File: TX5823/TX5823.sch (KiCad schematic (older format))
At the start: 8 parts

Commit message: an Schaltplan weitergearbeitet
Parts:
- added C? (x10): 100nF, Capacitors_SMD:C_0402, symbol C
- added C? (x5): 1uF, Capacitors_SMD:C_0603, symbol C
- added C?: 10uF, Capacitors_SMD:C_1206, symbol C
- added C?: Cboot, symbol C
- added C? (x2): 47uF, symbol CP2
- added C?: Cout, symbol CP2
- added C?: Cvccx, symbol C
- added C?: 100nF, symbol C
- added C?: Cvcc, symbol C
- added C?: Ccomp2, symbol C
- added C?: Ccomp, symbol C
- added C?: Css, symbol C
- added C?: Cramp, symbol C
- added C?: Cinx, symbol C
- added C?: Cin, symbol C
- added D?: LED, symbol LED
- added D? (x4): DIODESCH, symbol DIODESCH
- added L?: 15uH, symbol INDUCTOR
- added P?: CONN_02X03, symbol CONN_02X03
- added Q?: MOSFET_N, symbol MOSFET_N
- added Q? (x2): MOS_N, symbol MOS_N
- added R?: 10, symbol R
- added R?: 100, Resistors_SMD:R_1206, symbol R
- added R? (x4): open, Resistors_SMD:R_0402, symbol R
- added R?: 10k, symbol R
- added R?: 330, symbol R
- added R? (x2): 75, symbol R
- added R?: Rsense, symbol R
- added R?: Rfbt, symbol R
- added R?: Rfbb, symbol R
- added R?: Rcomp, symbol R
- added R?: Rt, symbol R
- added R?: Renable, symbol R
- added R?: Ruv1, symbol R
- added R?: Ruv2, symbol R
- added RP?: R_PACK4, symbol R_PACK4
- added SW?: SW_PUSH, symbol SW_PUSH
- added X?: 27MHz, symbol CRYSTAL_SMD
- added Y?: 16MHz, symbol RESONATEUR
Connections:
- net +3.3V: now also IC?.8 (VCC), U?.1 (SNS), U?.15 (OUT), U?.16 (OUT), U?.4 (3,3V_VCC), C?.1, C?.1, C?.1, C?.1, C?.1
- net GND: now reaches U?.3 (GND)
- net GND: now also IC?.21 (GND), IC?.3 (GND), IC?.4 (GND), IC?.5 (GND), U?.10 (1,6V), U?.13 (CSG), U?.14 (PGND), U?.17 (EP), U?.20 (AGND), U?.21 (EP), U?.23 (PGND), U?.27, U?.4 (DGND), U?.5 (GND), U?.6 (AGND), U?.7 (GND), U?.8 (400mV), U?.9 (800mV), U?.9 (GND), C?.1, C?.2, C?.2, C?.2, C?.2, C?.2, C?.2, C?.2, C?.2, C?.2, C?.2, C?.2, C?.2, C?.2, C?.2, C?.2, C?.2, C?.2, C?.2, C?.2, D?.2 (K), P?.6 (P6), Q?.S, Q?.S, R?.1, R?.2, R?.2, R?.2, R?.2, R?.2, R?.2, R?.2, SW?.2, Y?.2
- net SCK: now reaches U?.10 (SCLK)
- net SCK: now also IC?.17 ((PCINT5/SCK)PB5), P?.3 (P3), R?.1
- net MISO: now reaches U?.11 (SDOUT)
- net MISO: now also IC?.16 ((PCINT4/MISO)PB4), P?.1 (P1)
- net LOS: now reaches U?.12 (LOS)
- net LOS: now also RP?.7 (R2)
- net VSYNC: now reaches U?.17 (~VSYNC)
- net VSYNC: now also IC?.32 ((PCINT18/INT0)PD2), RP?.6 (R3)
- net HSYNC: now reaches U?.18 (~HSYNC)
- net HSYNC: now also RP?.5 (R4)
- net RESET: now reaches U?.19 (~RESET)
- net RESET: now also IC?.29 ((PCINT14/~RESET~)PC6), C?.1, P?.5 (P5), R?.2, SW?.1
- net +5V: now reaches U?.21 (AVDD)
- net +5V: now also IC?.18 (AVCC), IC?.4 (VCC), IC?.6 (VCC), U?.12 (EN), U?.13 (IN), U?.14 (IN), U?.24 (PVDD), U?.3 (DVDD), C?.1, C?.1, C?.1, C?.1, C?.1, C?.1, C?.1, P?.2 (P2), R?.1, R?.1, R?.1, RP?.2 (P2), RP?.3 (P3), RP?.4 (P4)
- net at U?.22 (VIN): now also C?.2
- net at U?.25 (SAG): now also C?.2
- net at U?.26 (VOUT): now also C?.2
- net at U?.5 (CLKIN): now also X?.1
- net at U?.6 (XFB): now also X?.2
- net CLKOUT: now reaches U?.7 (CLKOUT)
- net SSOD-IN: now reaches U?.8 (~CS)
- net MOSI: now reaches U?.9 (SDIN)
- net MOSI: now also IC?.15 ((PCINT3/OC2A/MOSI)PB3), P?.4 (P4)
- net PAL: now reaches IC?.1 ((PCINT19/OC2B/INT1)PD3)
- net PAL: now also R?.2
- net SSOSD-IN: now reaches IC?.10 ((PCINT22/OC0A/AIN0)PD6)
- net at IC?.20 (AREF): now also C?.1
- net RXI: now reaches IC?.30 ((PCINT16/RXD)PD0)
- net TXO: now reaches IC?.31 ((PCINT17/TXD)PD1)
- net at IC?.7 ((PCINT6/XTAL1/TOSC1)PB6): now also Y?.3
- net at IC?.8 ((PCINT7/XTAL2/TOSC2)PB7): now also Y?.1
- net at IC?.2 (PB3(CLKI/ADC3/PCINT3)): now also R?.1
- net PWM_in: now reaches IC?.6 (PB1(MISO/AIN1/OC0B/INT0/PCINT1))
- net at U?.11 (SS): now also C?.1
- net at U?.2 (FB): now also C?.2, C?.2
- net at U?.4 (50mV): now also R?.1
- net at U?.5 (100mV): now also R?.1
- net at U?.6 (200mV): now also R?.1
- net at U?.1 (VIN): now also C?.1, C?.1, Q?.D, R?.1, R?.1
- net at U?.10 (VOUT): now also C?.1, D?.2 (K), D?.2 (K), R?.1
- net at U?.12 (CS): now also D?.1 (A), D?.1 (A), R?.1
- net at U?.15 (LO): now also Q?.G
- net at U?.16 (VCC): now also C?.1
- net at U?.17 (VCCX): now also C?.2
- net at U?.18 (HB): now also C?.2
- net at U?.19 (HO): now also Q?.G
- net at U?.2 (UVLO): now also R?.1, R?.2
- net at U?.20 (HS): now also C?.1, D?.2 (K), D?.2 (K), L?.1, Q?.S
- net at U?.3 (RT): now also R?.1
- net at U?.4 (EN): now also R?.2
- net at U?.5 (RAMP): now also C?.1
- net at U?.7 (SS): now also C?.1
- net at U?.8 (FB): now also C?.2, C?.2, R?.2, R?.2
- net at U?.9 (COMP): now also C?.1, R?.1
- new net: Q?.G, R?.2
- new net: D?.1 (A), R?.2
- new net: D?.1 (A), D?.1 (A), L?.2, Q?.D
- new net: C?.1, C?.1, R?.2
- new net: C?.1, R?.2
- new net DTR: C?.2
- new net IR_LED+: R?.2
- new net IR_LED-: Q?.D
- new net VIN: C?.1, R?.1
- new net VOUT: R?.1
- no-connect marks 0 -> 17
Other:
- note added: "12V Buck Boost\nVinMin 8V\nVinMax=30V\nVout=12V\nIout= 2A"
- note added: "5V Stepdown"
- note added: "FPV Sender\nund 3,3V"
- note added: "OSD"
- note removed: "5V_Stepdown"
- note removed: "TODO\nBOOST\nEP anpassen\n"
- moved on the sheet: IC?, R?, U?

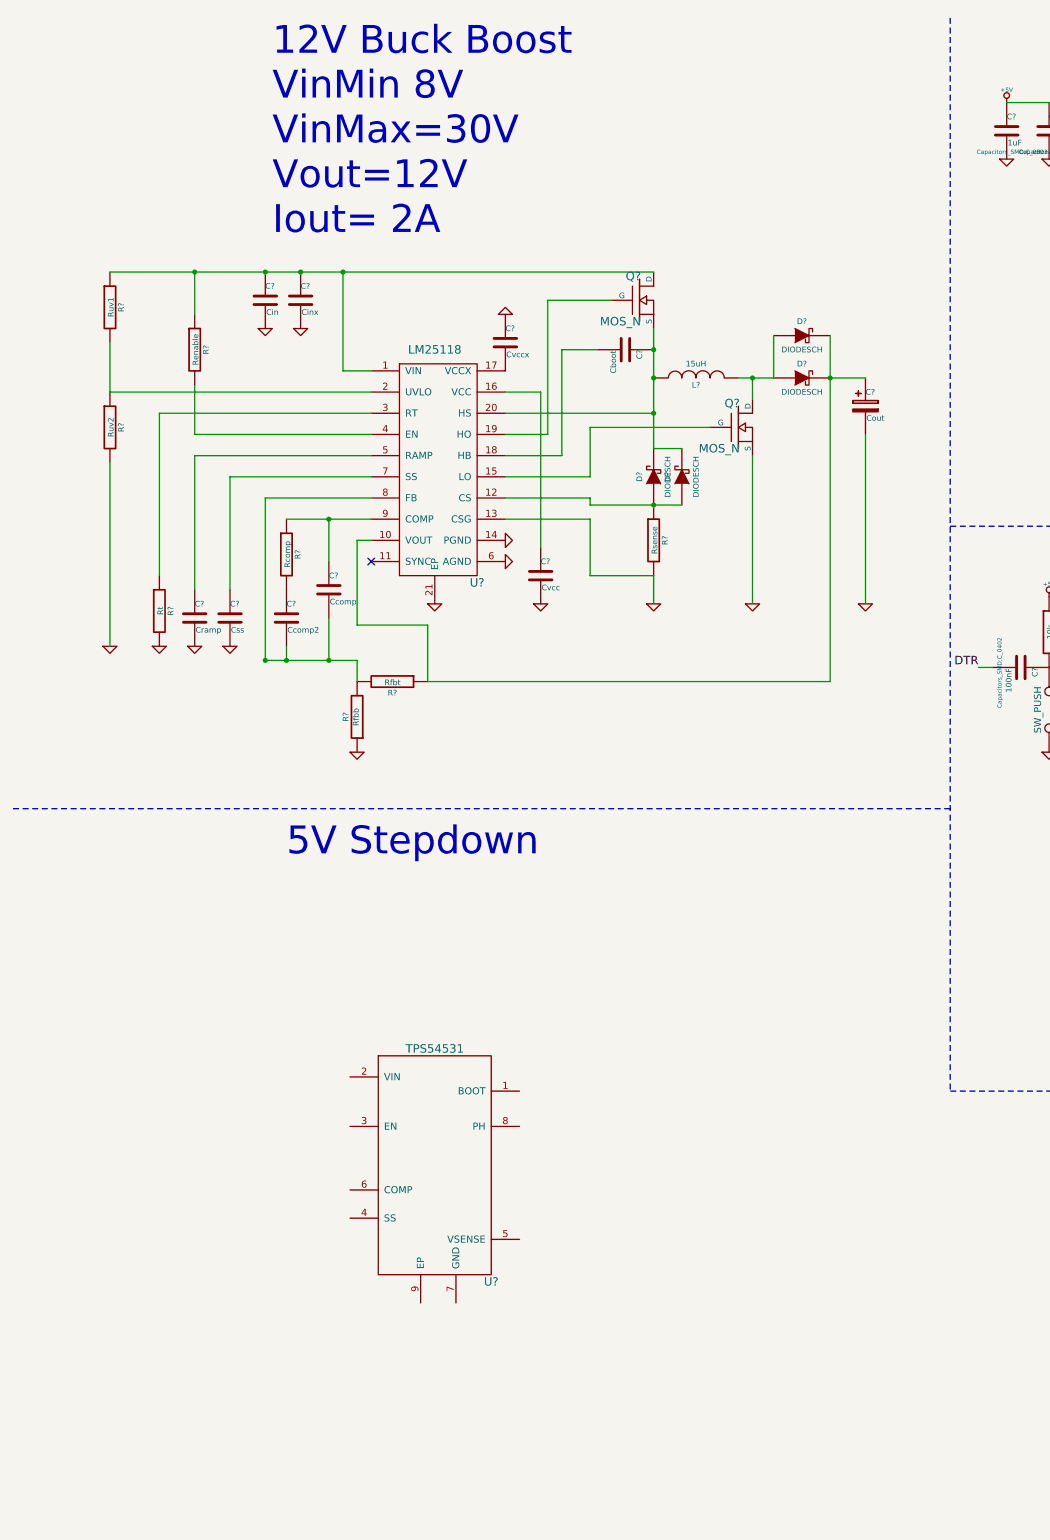
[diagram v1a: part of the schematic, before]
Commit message: an Schaltplan weitergearbeitet. 5V Buck
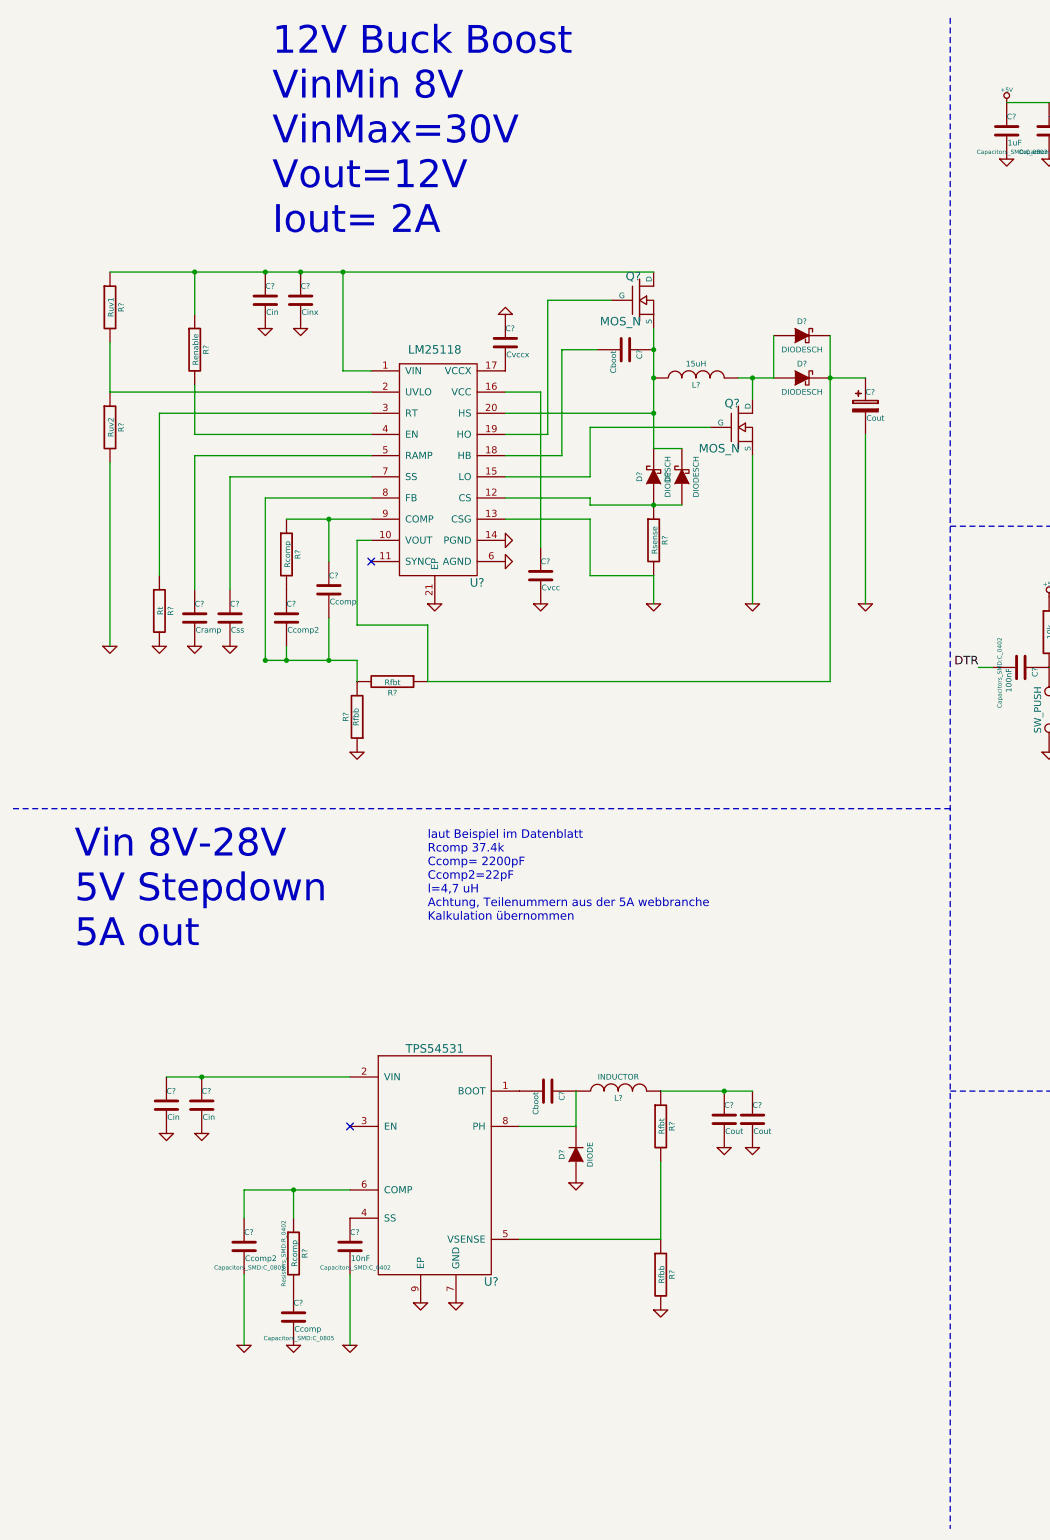
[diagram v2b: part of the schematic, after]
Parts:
- added C?: Cboot, symbol C
- added C? (x2): Cout, symbol C
- added C?: 10nF, Capacitors_SMD:C_0402, symbol C
- added C?: Ccomp, Capacitors_SMD:C_0805, symbol C
- added C?: Ccomp2, Capacitors_SMD:C_0805, symbol C
- added C? (x2): Cin, symbol C
- added D?: DIODE, symbol DIODE
- added L?: INDUCTOR, symbol INDUCTOR
- added R?: Rfbt, symbol R
- added R?: Rfbb, symbol R
- added R?: Rcomp, Resistors_SMD:R_0402, symbol R
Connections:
- net GND: now also U?.7 (GND), U?.9 (EP), C?.2, C?.2, C?.2, C?.2, C?.2, C?.2, C?.2, D?.1 (A), R?.2
- net at U?.1 (BOOT): now also C?.2
- net at U?.2 (VIN): now also C?.1, C?.1
- net at U?.4 (SS): now also C?.1
- net at U?.5 (VSENSE): now also R?.1, R?.2
- net at U?.6 (COMP): now also C?.1, R?.1
- net at U?.8 (PH): now also C?.1, D?.2 (K), L?.1
- new net: C?.1, C?.1, L?.2, R?.1
- new net: C?.1, R?.2
- no-connect marks 17 -> 18
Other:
- note added: "Vin 8V-28V\n5V Stepdown\n5A out"
- note added: "laut Beispiel im Datenblatt\nRcomp 37.4k\nCcomp= 2200pF\nCcomp2=22pF\nl=4,7 uH\nAchtung, Teilenummern aus der 5A webbranche\nKalkulation übernommen\n\n"
- note removed: "5V Stepdown"

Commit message: Teilenummern und connectoren hinzugefügt
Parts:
- added P?: Mavlink, symbol CONN_01X05
- added R? (x3): open, Resistors_SMD:R_0603, symbol R
- added R?: 0R, Resistors_SMD:R_0603, symbol R
- added R?: R, symbol R
- added U?: CONN_03X08, symbol CONN_03X08
- added U?: OPTO-TRANSISTOR4, symbol OPTO-TRANSISTOR4
- C?: footprint (none) -> Capacitors_SMD:C_0402
- C? (x4): footprint (none) -> Capacitors_SMD:C_1210
- R? (x2): footprint (none) -> Resistors_SMD:R_0402
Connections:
- net VOUT is gone; now on net VIDEO_OUT_OSD: R?.1
- net +3.3V: now also R?.1
- net +5V: now also C?.1, C?.1, L?.2, R?.1, R?.1, U?.14 (5_2), U?.17 (6_2)
- net GND: now also U?.1 (1_1), U?.13 (5_1), U?.16 (6_1), U?.19 (7_1), U?.22 (8_1), U?.3 (E), U?.4 (2_1)
- net IR_LED+: now also U?.12 (4_3)
- net IR_LED-: now also U?.10 (4_1)
- net VIDEO_OUT_OSD: now reaches U?.1 (VIDEO_IN)
- net VIDEO_OUT_OSD: now also R?.1
- net AUDIO_IN_TX: now reaches U?.2 (AUDIO_RO)
- net AUDIO_IN_TX: now also U?.6 (2_3)
- net +12V: now reaches C?.1, D?.2 (K), D?.2 (K), R?.1, U?.10 (VOUT)
- net +12V: now also R?.1, U?.20 (7_2), U?.23 (8_2)
- net VIN renamed VIDEO_IN_OSD
- net VIDEO_IN_OSD: now also R?.1
- new net: R?.2, R?.2, U?.2 (1_2)
- new net: R?.2, R?.2, U?.3 (1_3)
- new net: U?.2 (K), U?.7 (3_1)
- new net: U?.1 (A), U?.9 (3_3)
- new net: R?.2, U?.4 (C)
- no-connect marks 18 -> 25
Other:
- note added: "1 :Video in\n2: Sound in\n3: PWM in\n4: Infrarot out\n5: 5V\n6: 5V\n7: 12V\n8: 12V"

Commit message: an Steckern im Schaltplan weitergearbeitet
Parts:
- removed R?: R, symbol R
- added R?: 100R, symbol R
- added R? (x2): 300R, symbol R
- added R?: open, Resistors_SMD:R_0603, symbol R
- added SW?: SW_PUSH, symbol SW_PUSH
- added U?: OPTO-TRANSISTOR4, symbol OPTO-TRANSISTOR4
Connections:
- net +5V: now also P?.4 (P4), R?.1
- net DTR: now also P?.1 (P1)
- net GND: now also SW?.1, U?.3 (E)
- net PWM_in: now also U?.4 (C)
- net RXI: now also R?.2, U?.4 (C)
- net TXO: now also R?.2
- net at U?.9 (3_3): now also R?.2; no longer U?.1 (A)
- net at P?.2 (P2): now also R?.1
- net at P?.3 (P3): now also R?.1
- net at P?.5 (P5): now also SW?.2, U?.2 (K)
- new net: R?.1, U?.1 (A)
- new net: R?.2, U?.1 (A)
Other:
- moved on the sheet: P?
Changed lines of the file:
@@
 	0    1    1    0
 $EndComp
-Text Label 15800 6100 0    60   ~ 0
+Text Label 15800 6100 1    60   ~ 0
 VIDEO_OUT_OSD
 $Comp
@@
 	1    0    0    -1
 $EndComp
-Text Label 15750 6900 0    60   ~ 0
+Text Label 15750 6900 1    60   ~ 0
 VIDEO_IN_OSD
 $Comp
@@
 Connection ~ 2750 4050
 Wire Wire Line
-	2750 4750 2750 5050
+	2750 5050 2750 4750
 Connection ~ 2750 5050
 Wire Wire Line
@@
 	2900 9400 2900 9900
 Wire Wire Line
-	2900 8800 2150 8800
+	2150 8800 2900 8800
 Wire Wire Line
 	2150 8800 2150 9000
@@
 	8650 10100 8650 9800
 Wire Wire Line
-	9000 9100 9000 10100
-Wire Wire Line
-	8800 8950 8800 10100
+	9000 9150 9000 10100
 Wire Wire Line
 	9350 10100 9350 9800
@@
 L CONN_01X05 P?
 U 1 1 5517FDD8
-P 12900 9600
-F 0 "P?" H 12900 9900 50  0000 C CNN
-F 1 "Mavlink" V 13000 9600 50  0000 C CNN
-F 2 "" H 12900 9600 60  0000 C CNN
-F 3 "" H 12900 9600 60  0000 C CNN
-	1    12900 9600
-	0    1    1    0
+P 15050 8900
+F 0 "P?" H 15050 9200 50  0000 C CNN
+F 1 "Mavlink" V 15150 8900 50  0000 C CNN
+F 2 "" H 15050 8900 60  0000 C CNN
+F 3 "" H 15050 8900 60  0000 C CNN
+	1    15050 8900
+	1    0    0    -1
 $EndComp
 $Comp
@@
 	8800 8950 8950 8950
 Wire Wire Line
-	9000 9100 8700 9100
-Wire Wire Line
-	8700 9100 8700 8650
-Wire Wire Line
-	8700 8650 8950 8650
-$Comp
-L +3,3V #PWR?
-U 1 1 551837B0
-P 10700 8650
-F 0 "#PWR?" H 10700 8610 30  0001 C CNN
-F 1 "+3,3V" H 10700 8760 30  0000 C CNN
-F 2 "" H 10700 8650 60  0000 C CNN
-F 3 "" H 10700 8650 60  0000 C CNN
-	1    10700 8650
-	1    0    0    -1
-$EndComp
-$Comp
-L R R?
-U 1 1 55184926
-P 10450 8650
-F 0 "R?" V 10530 8650 40  0000 C CNN
-F 1 "R" V 10457 8651 40  0000 C CNN
-F 2 "" V 10380 8650 30  0000 C CNN
-F 3 "" V 10530 8650 30  0000 C CNN
-	1    10450 8650
-	0    1    1    0
-$EndComp
-Wire Wire Line
-	10200 8650 10200 8500
+	9000 9150 8700 9150
 $Comp
 L GND #PWR?
@@
 Text Label 9350 9800 1    60   ~ 0
 IR_LED+
+Text Label 14850 8700 2    60   ~ 0
+DTR
+Text Label 14350 8800 2    60   ~ 0
+TXO
+Text Label 13100 8900 2    60   ~ 0
+RXI
+$Comp
+L +5V #PWR?
+U 1 1 55194093
+P 14850 9000
+F 0 "#PWR?" H 14850 9090 20  0001 C CNN
+F 1 "+5V" H 14850 9090 30  0000 C CNN
+F 2 "" H 14850 9000 60  0000 C CNN
+F 3 "" H 14850 9000 60  0000 C CNN
+	1    14850 9000
+	0    -1   -1   0
+$EndComp
+$Comp
+L R R?
+U 1 1 551949B3
+P 14600 8800
+F 0 "R?" V 14680 8800 40  0000 C CNN
+F 1 "100R" V 14607 8801 40  0000 C CNN
+F 2 "" V 14530 8800 30  0000 C CNN
+F 3 "" V 14680 8800 30  0000 C CNN
+	1    14600 8800
+	0    1    1    0
+$EndComp
+$Comp
+L OPTO-TRANSISTOR4 U?
+U 1 1 5519658E
+P 13700 9050
+F 0 "U?" H 13900 9300 60  0000 C CNN
+F 1 "OPTO-TRANSISTOR4" H 13700 8800 60  0000 C CNN
+F 2 "" H 13700 9050 60  0000 C CNN
+F 3 "" H 13700 9050 60  0000 C CNN
+	1    13700 9050
+	-1   0    0    -1
+$EndComp
+$Comp
+L R R?
+U 1 1 5519688E
+P 8700 8900
+F 0 "R?" V 8780 8900 40  0000 C CNN
+F 1 "300R" V 8707 8901 40  0000 C CNN
+F 2 "" V 8630 8900 30  0000 C CNN
+F 3 "" V 8780 8900 30  0000 C CNN
+	1    8700 8900
+	1    0    0    -1
+$EndComp
+Wire Wire Line
+	8800 8950 8800 10100
+Wire Wire Line
+	8700 8650 8950 8650
+$Comp
+L R R?
+U 1 1 55197380
+P 14600 8900
+F 0 "R?" V 14680 8900 40  0000 C CNN
+F 1 "300R" V 14607 8901 40  0000 C CNN
+F 2 "" V 14530 8900 30  0000 C CNN
+F 3 "" V 14680 8900 30  0000 C CNN
+	1    14600 8900
+	0    1    1    0
+$EndComp
+Text Label 10200 8650 0    60   ~ 0
+PWM_in
+$Comp
+L +5V #PWR?
+U 1 1 55198D20
+P 13100 8400
+F 0 "#PWR?" H 13100 8490 20  0001 C CNN
+F 1 "+5V" H 13100 8490 30  0000 C CNN
+F 2 "" H 13100 8400 60  0000 C CNN
+F 3 "" H 13100 8400 60  0000 C CNN
+	1    13100 8400
+	1    0    0    -1
+$EndComp
+$Comp
+L R R?
+U 1 1 5519918F
+P 13100 8650
+F 0 "R?" V 13180 8650 40  0000 C CNN
+F 1 "open" V 13107 8651 40  0000 C CNN
+F 2 "Resistors_SMD:R_0603" V 13030 8650 30  0001 C CNN
+F 3 "" V 13180 8650 30  0000 C CNN
+	1    13100 8650
+	1    0    0    -1
+$EndComp
+$Comp
+L GND #PWR?
+U 1 1 55199759
+P 13100 9550
+F 0 "#PWR?" H 13100 9550 30  0001 C CNN
+F 1 "GND" H 13100 9480 30  0001 C CNN
+F 2 "" H 13100 9550 60  0000 C CNN
+F 3 "" H 13100 9550 60  0000 C CNN
+	1    13100 9550
+	1    0    0    -1
+$EndComp
+Wire Wire Line
+	14350 9200 14450 9200
+Wire Wire Line
+	14450 9200 14450 9100
+Wire Wire Line
+	14450 9100 14850 9100
+Connection ~ 13100 9500
+Wire Wire Line
+	13100 9200 13100 9550
+Wire Wire Line
+	13100 9500 13350 9500
+$Comp
+L SW_PUSH SW?
+U 1 1 5519BDF1
+P 13650 9500
+F 0 "SW?" H 13800 9610 50  0000 C CNN
+F 1 "SW_PUSH" H 13650 9420 50  0000 C CNN
+F 2 "" H 13650 9500 60  0000 C CNN
+F 3 "" H 13650 9500 60  0000 C CNN
+	1    13650 9500
+	1    0    0    -1
+$EndComp
+Wire Wire Line
+	14350 9500 14350 9200
+Wire Wire Line
+	13950 9500 14350 9500
 $EndSCHEMATC
